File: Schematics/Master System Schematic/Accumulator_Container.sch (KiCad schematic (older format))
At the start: 18 parts, among them J4 Shutdown/MC Control Connector, J5 TSMP/IMD Connector, J6 Main TS Connector, J7 TSAL Connector, K1 SPST-NO (Precharge), K2 SPST-NO (AIR), K3 SPST-NO (AIR), K4 SPST-NC (Discharge), K5 SPST-NO (Precharge Control), K6 SPST-NO (AIR Control), U5 OrionCurrentSens

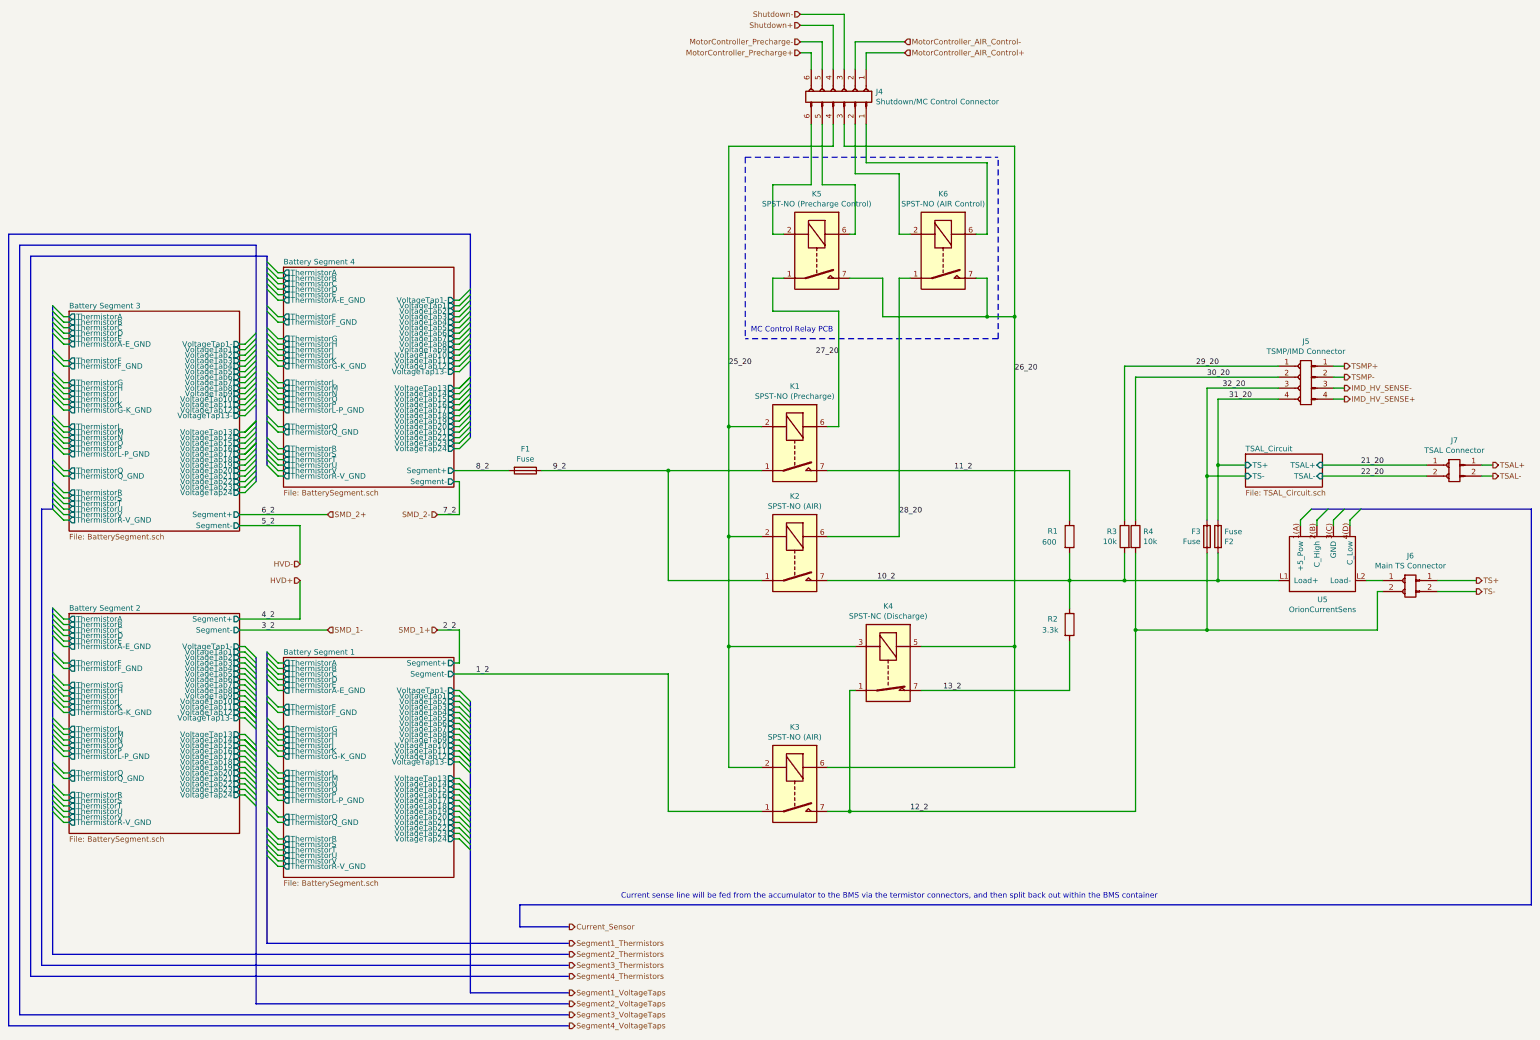
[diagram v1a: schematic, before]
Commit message: Started Voltage tap pcbs
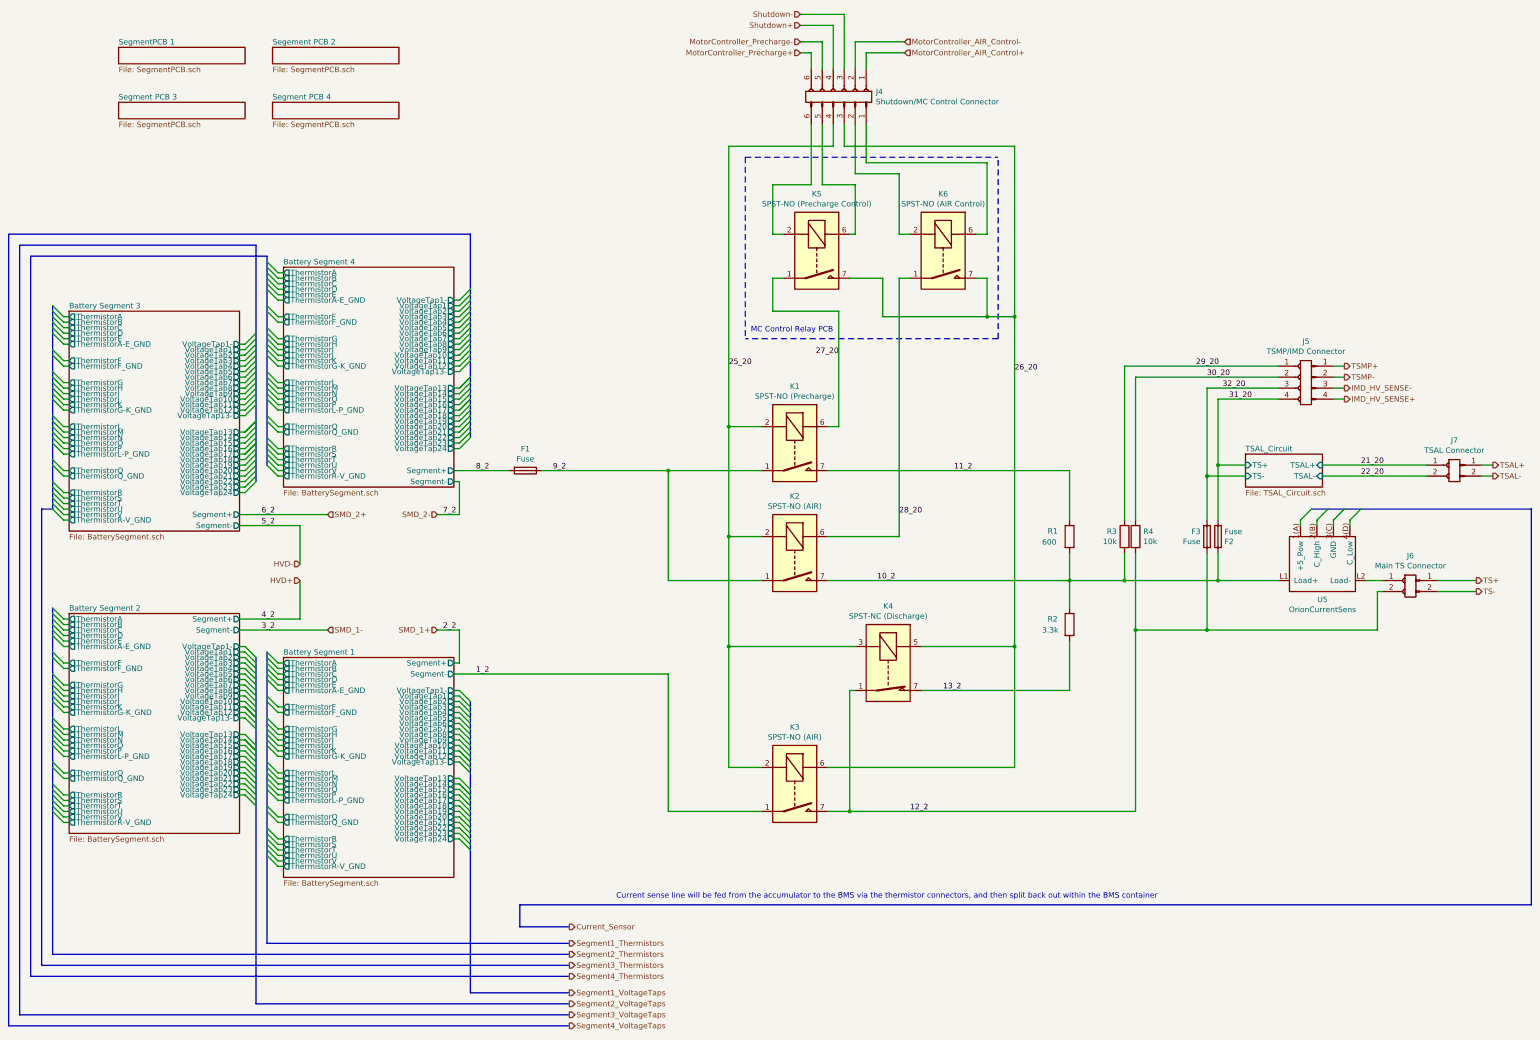
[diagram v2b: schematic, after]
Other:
- note added: "Current sense line will be fed from the accumulator to the BMS via the thermistor connectors, and then split back out within the BMS container"
- note removed: "Current sense line will be fed from the accumulator to the BMS via the termistor connectors, and then split back out within the BMS container"
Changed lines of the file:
@@
 $Descr B 17000 11000
 encoding utf-8
-Sheet 8 13
+Sheet 8 17
 Title "Accumulator Container"
 Date "2020-10-12"
@@
 	15300 5350 15300 8950
 Text Notes 11900 8900 2    50   ~ 0
-Current sense line will be fed from the accumulator to the BMS via the termistor connectors, and then split back out within the BMS container
+Current sense line will be fed from the accumulator to the BMS via the thermistor connectors, and then split back out within the BMS container
 Wire Bus Line
 	1650 9600 6550 9600
@@
 Text HLabel 6550 9150 2    50   Output ~ 0
 Current_Sensor
+$Sheet
+S 2450 1150 1150 150
+U 604010F7
+F0 "SegmentPCB 1" 50
+F1 "SegmentPCB.sch" 50
+$EndSheet
+$Sheet
+S 3850 1150 1150 150
+U 604B77CB
+F0 "Segement PCB 2" 50
+F1 "SegmentPCB.sch" 50
+$EndSheet
+$Sheet
+S 2450 1650 1150 150
+U 604E5331
+F0 "Segment PCB 3" 50
+F1 "SegmentPCB.sch" 50
+$EndSheet
+$Sheet
+S 3850 1650 1150 150
+U 604E5333
+F0 "Segment PCB 4" 50
+F1 "SegmentPCB.sch" 50
+$EndSheet
 Wire Bus Line
 	13300 5350 15300 5350

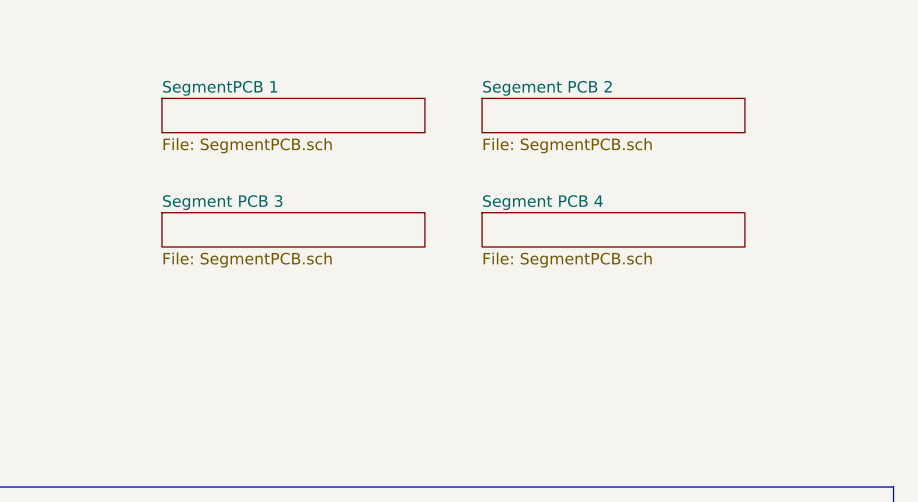
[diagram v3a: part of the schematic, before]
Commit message: Clean up for merge
>cleaned wire runs on top sheet
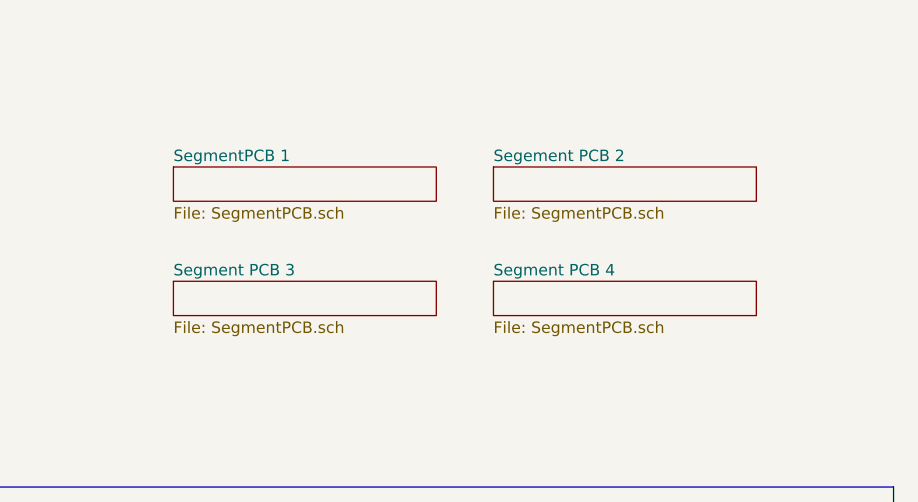
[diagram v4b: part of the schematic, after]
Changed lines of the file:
@@
 EESchema Schematic File Version 4
-LIBS:Master System Schematic-cache
 EELAYER 30 0
 EELAYER END
 $Descr B 17000 11000
 encoding utf-8
-Sheet 8 17
+Sheet 7 17
 Title "Accumulator Container"
 Date "2020-10-12"
@@
 Current_Sensor
 $Sheet
-S 2450 1150 1150 150
+S 2500 1450 1150 150
 U 604010F7
 F0 "SegmentPCB 1" 50
@@
 $EndSheet
 $Sheet
-S 3850 1150 1150 150
+S 3900 1450 1150 150
 U 604B77CB
 F0 "Segement PCB 2" 50
@@
 $EndSheet
 $Sheet
-S 2450 1650 1150 150
+S 2500 1950 1150 150
 U 604E5331
 F0 "Segment PCB 3" 50
@@
 $EndSheet
 $Sheet
-S 3850 1650 1150 150
+S 3900 1950 1150 150
 U 604E5333
 F0 "Segment PCB 4" 50
